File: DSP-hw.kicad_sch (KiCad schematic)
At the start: 0 parts

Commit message: Iniziata un po la schematica
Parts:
- added C1, C12, C14, C16, C18, C21, C3, C6, C9: 100n, Capacitor_SMD:C_0603_1608Metric, symbol Device:C
- added C10, C13, C15, C17, C2, C4, C5, C8: 10u, Capacitor_SMD:C_0603_1608Metric, symbol Device:C
- added C11, C7: 1u, Capacitor_SMD:C_0603_1608Metric, symbol Device:C
- added C19, C20: 47u, Capacitor_SMD:C_0603_1608Metric, symbol Device:C
- added C22, C23: 22p, Capacitor_SMD:C_0603_1608Metric, symbol Device:C
- added Q1: BC327, Package_TO_SOT_THT:TO-92_Inline, symbol Transistor_BJT:BC327
- added R1: 1k, Resistor_SMD:R_0603_1608Metric, symbol Device:R
- added R2, R3, R7: 33, Resistor_SMD:R_0603_1608Metric, symbol Device:R
- added R4: 2k2, Resistor_SMD:R_0603_1608Metric, symbol Device:R
- added R5: 18k, Resistor_SMD:R_0603_1608Metric, symbol Device:R
- added R6: 100, Resistor_SMD:R_0603_1608Metric, symbol Device:R
- added R8: 10k, Resistor_SMD:R_0603_1608Metric, symbol Device:R
- added SW1: SW_Push, Button_Switch_SMD:SW_SPST_PTS645Sx43SMTR92, symbol Switch:SW_Push
- added U1: ADAU1701, Package_QFP:LQFP-48_7x7mm_P0.5mm, symbol DSP_AnalogDevices:ADAU1701
- added U2: CAT24C256, Package_SO:SOIC-8_3.9x4.9mm_P1.27mm, symbol Memory_EEPROM:CAT24C256
- added U3: AMS1117-3.3, Package_TO_SOT_SMD:SOT-223-3_TabPin2, symbol Regulator_Linear:AMS1117-3.3
- added Y1: 12.228M, Crystal:Crystal_SMD_HC49-SD, symbol Device:Crystal
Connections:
- new net: R2.1, U2.5 (SDA)
- new net: R3.1, U2.6 (SCL)
- new net: C16.1, C17.1, U1.40 (CM)
- new net: C23.2, R6.1, Y1.2
- new net: R6.2, U1.31 (OSCO)
- new net: C5.2, C6.2, C7.2, C8.2, U1.34 (PVDD), U1.36 (AVDD), U1.48 (AVDD)
- new net: R5.2, U1.3 (ADC_RES)
- new net: R7.1, R8.1, SW1.2
- new net: R7.2, U1.5 (~{RESET})
- new net: C1.1, C2.1, C3.1, C4.1, Q1.1 (C), U1.13 (DVDD), U1.24 (DVDD)
- new net: C22.2, U1.32 (MCLKI), Y1.1
- new net: C14.1, C15.1, U1.47 (FILTA)
- new net: C12.1, C13.1, U1.41 (FILTD)
- new net +3V3: C10.2, C11.2, C18.1, C19.1, C9.2, Q1.2 (B), Q1.3 (E), R1.1, R1.2, R4.1, R8.2, U1.17 (VDRIVE), U1.18 (IOVDD), U1.39 (PLL_MODE1), U1.6 (SELFBOOT), U2.8 (VCC), U3.2 (VO)
- new net +5V: C20.1, C21.1, U3.3 (VI)
- new net ADC0: U1.2 (ADC0)
- new net ADC1: U1.4 (ADC1)
- new net BCLK: U1.9 (MP5)
- new net DAC0: U1.46 (VOUT0)
- new net DAC1: U1.45 (VOUT1)
- new net DAC2: U1.44 (VOUT2)
- new net DAC3: U1.43 (VOUT3)
- new net DIN: U1.15 (MP6)
- new net DOUT: U1.11 (MP0)
- new net GND: C1.2, C10.1, C11.1, C12.2, C13.2, C14.2, C15.2, C16.2, C17.2, C18.2, C19.2, C2.2, C20.2, C21.2, C22.1, C23.1, C3.2, C4.2, C5.1, C6.1, C7.1, C8.1, C9.1, R5.1, SW1.1, U1.1 (AGND), U1.12 (DGND), U1.25 (DGND), U1.30 (RSVD), U1.33 (PGND), U1.37 (AGND), U1.38 (PLL_MODE0), U1.42 (AGND), U1.7 (ADDR0), U2.1 (A0), U2.2 (A1), U2.3 (A2), U2.4 (GND), U3.1 (GND)
- new net LRCLK: U1.8 (MP4)
- new net SCL: R3.2, U1.23 (SCL/CCLK)
- new net SDA: R2.2, U1.22 (SDA/COUT)
- new net WP: R4.2, U1.21 (CLATCH/WP), U2.7 (WP)

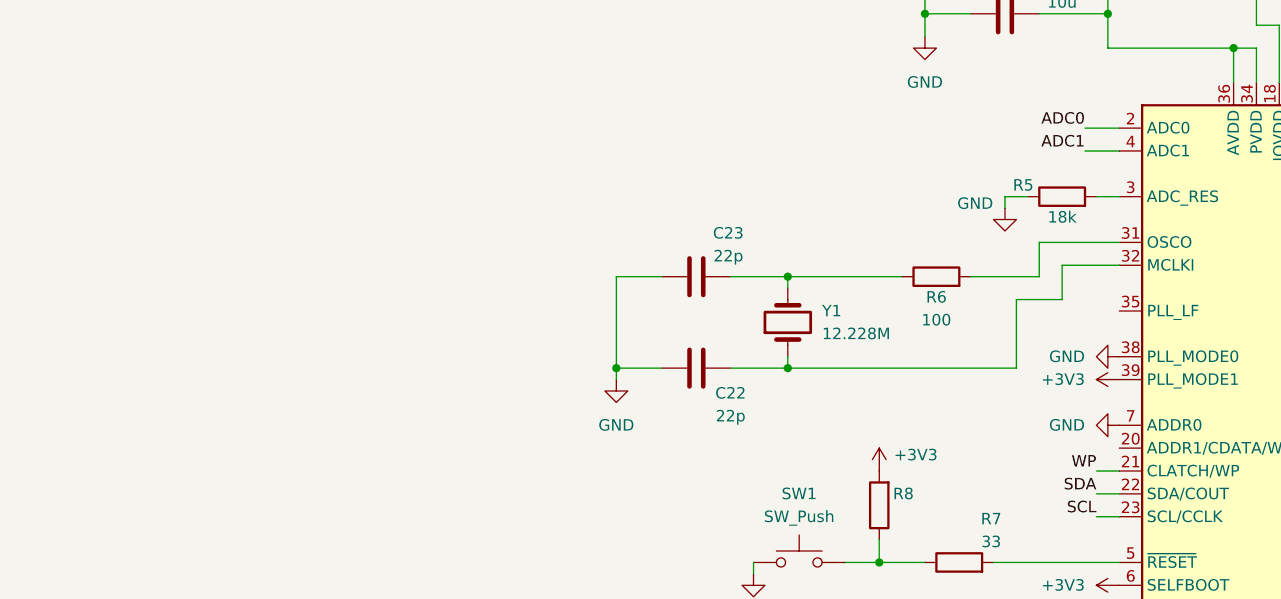
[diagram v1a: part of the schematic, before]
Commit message: aggiunto filtro PLL_LF Adau
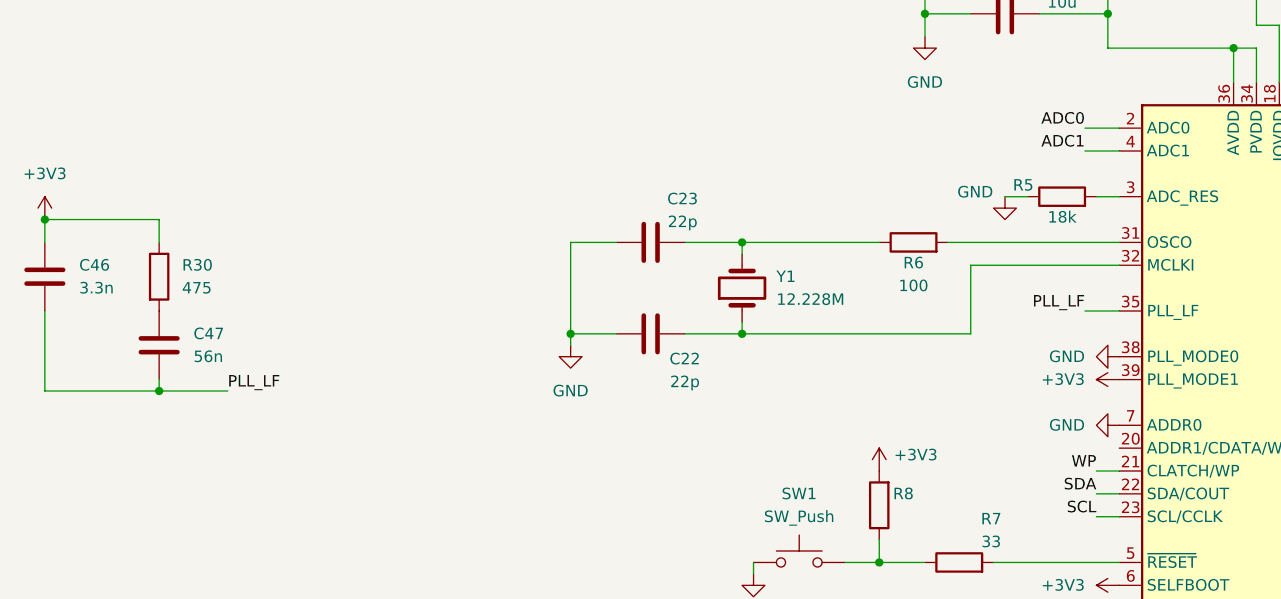
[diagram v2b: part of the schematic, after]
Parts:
- added C46: 3.3n, Capacitor_SMD:C_0603_1608Metric, symbol Device:C
- added C47: 56n, Capacitor_SMD:C_0603_1608Metric, symbol Device:C
- added R30: 475, Resistor_SMD:R_0603_1608Metric, symbol Device:R
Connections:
- net +3V3: now also C46.1, R30.1
- net PLL_LF: now reaches U1.35 (PLL_LF)
- net PLL_LF: now also C46.2, C47.2
- new net: C47.1, R30.2
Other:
- moved on the sheet: C22, C23, R6, Y1

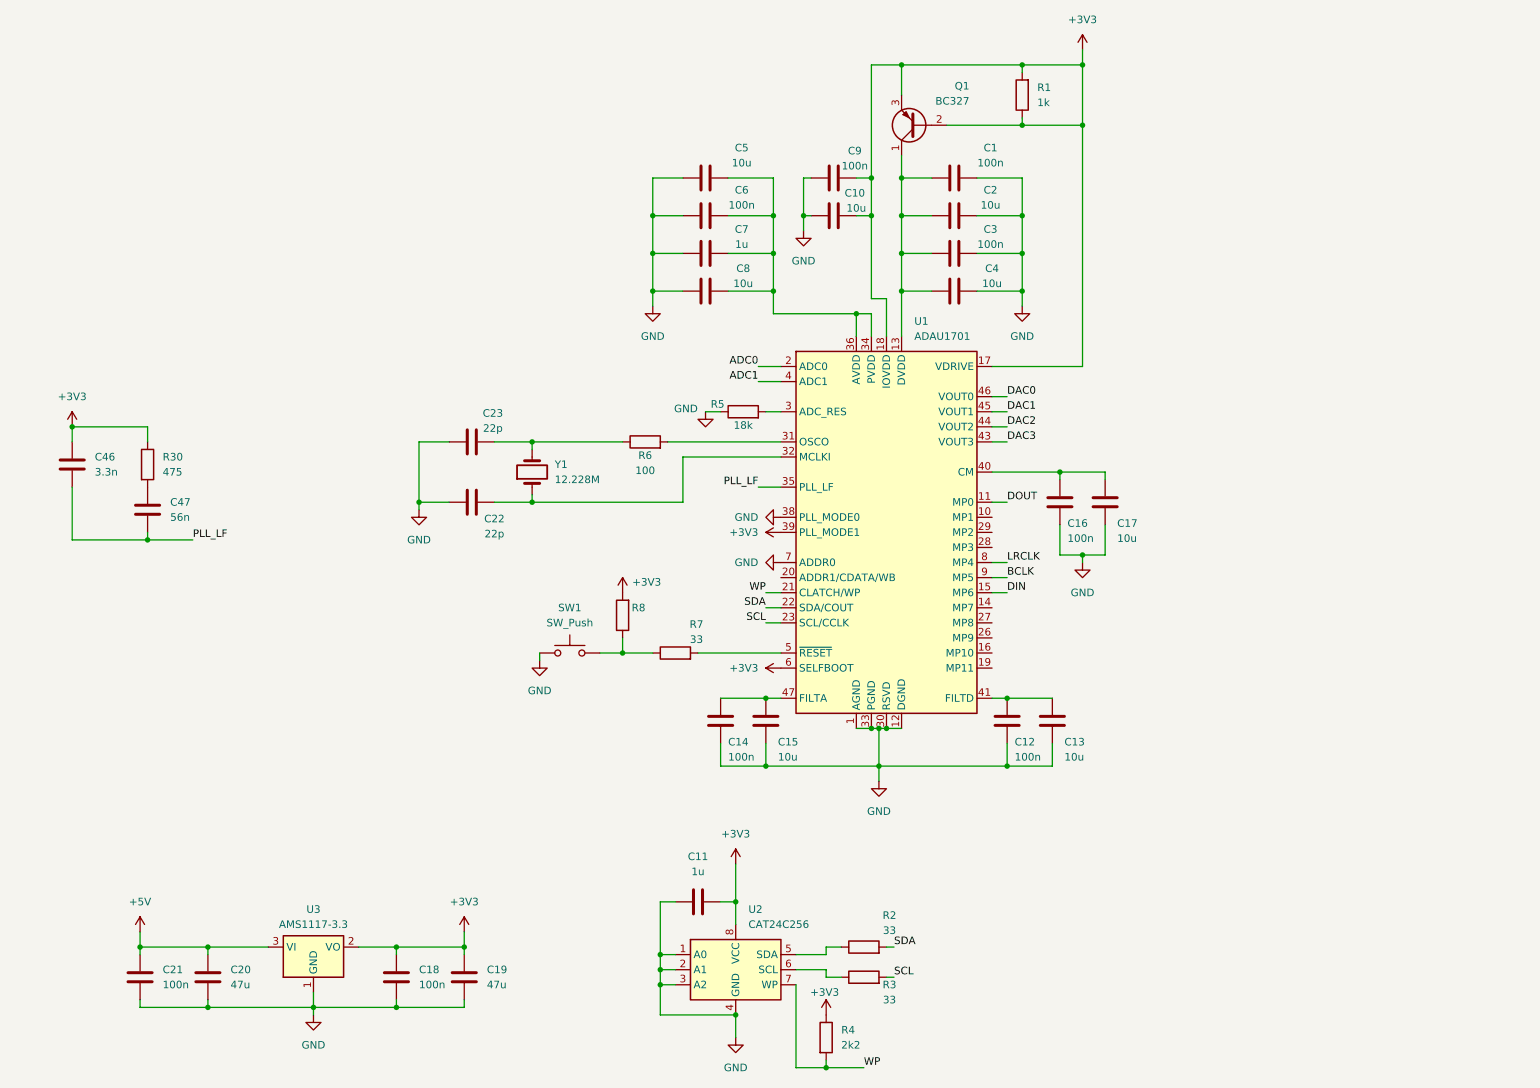
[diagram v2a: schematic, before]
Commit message: sostituito micro esp32 a stm32
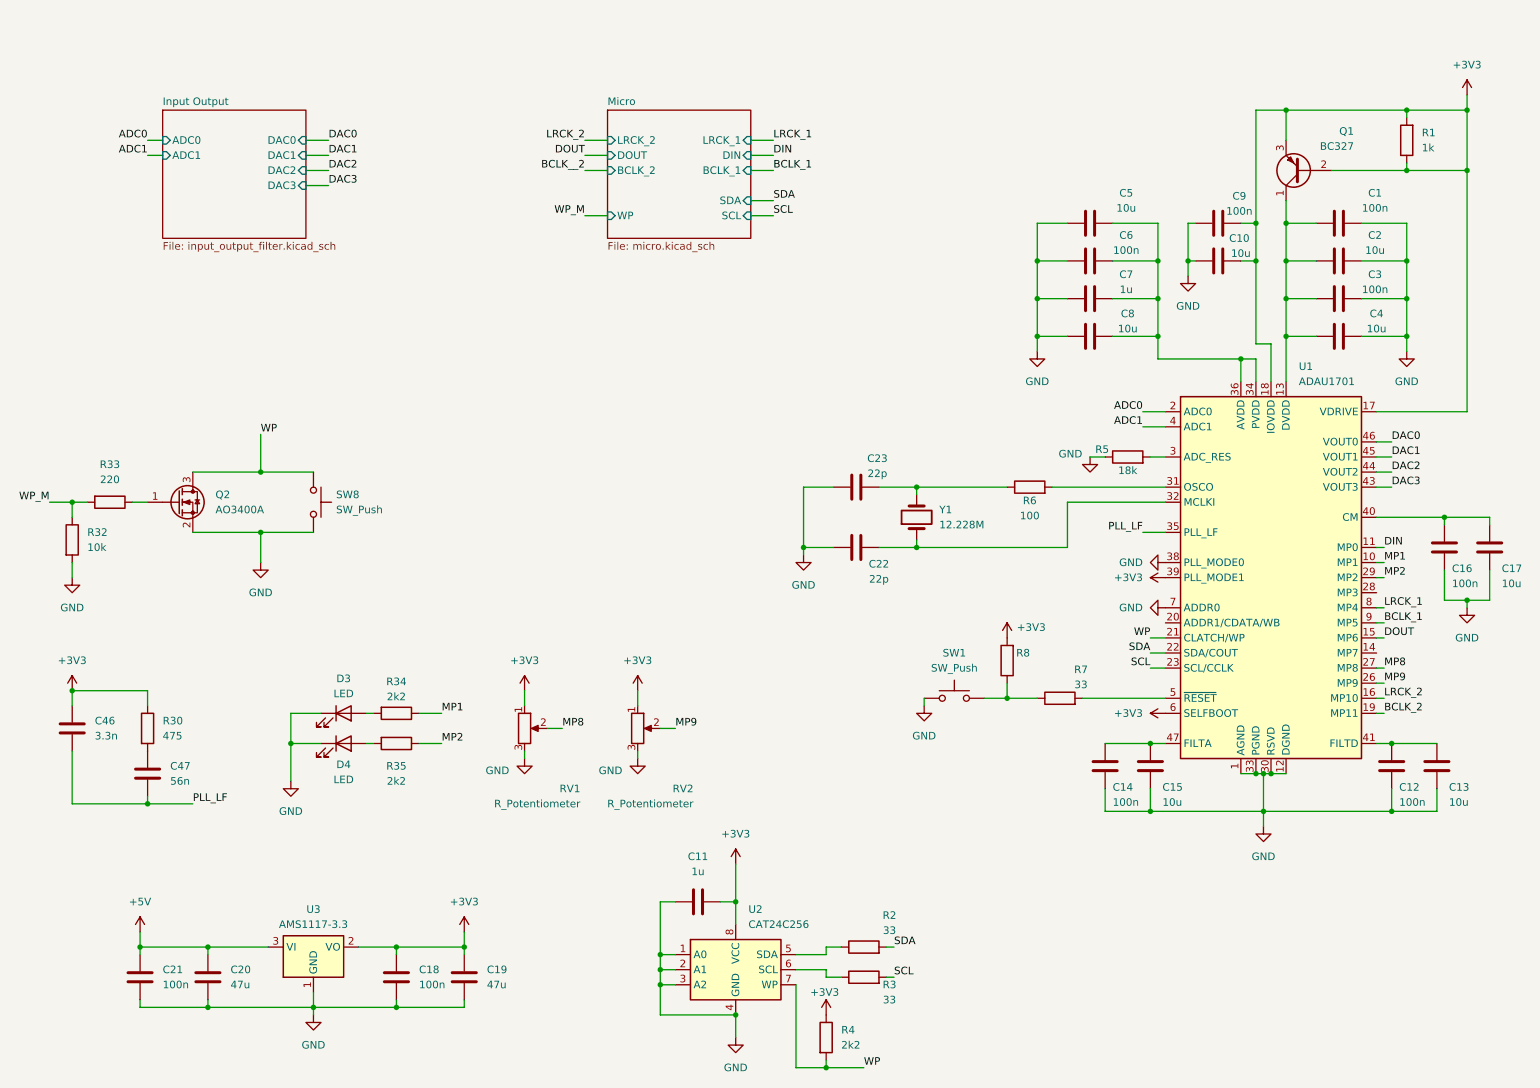
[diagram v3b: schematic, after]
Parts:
- added D3, D4: LED, LED_SMD:LED_1210_3225Metric, symbol Device:LED
- added Q2: AO3400A, Package_TO_SOT_SMD:SOT-23, symbol Transistor_FET:AO3400A
- added R32: 10k, Resistor_SMD:R_0603_1608Metric, symbol Device:R
- added R33: 220, Resistor_SMD:R_0603_1608Metric, symbol Device:R
- added R34, R35: 2k2, Resistor_SMD:R_0603_1608Metric, symbol Device:R
- added RV1, RV2: R_Potentiometer, Potentiometer_THT:Potentiometer_Alps_RK097_Single_Horizontal, symbol Device:R_Potentiometer
- added SW8: SW_Push, Button_Switch_SMD:SW_SPST_PTS645Sx43SMTR92, symbol Switch:SW_Push
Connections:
- net +3V3: now also RV1.1, RV2.1
- net DIN: now also U1.11 (MP0); no longer U1.15 (MP6)
- net DOUT: now also U1.15 (MP6); no longer U1.11 (MP0)
- net GND: now also D3.1 (K), D4.1 (K), Q2.2 (S), R32.2, RV1.3, RV2.3, SW8.2
- net WP: now also Q2.3 (D), SW8.1
- net MP1: now reaches U1.10 (MP1)
- net MP1: now also R34.1
- net LRCK_2: now reaches U1.16 (MP10)
- net BCLK_2: now reaches U1.19 (MP11)
- net MP9: now reaches U1.26 (MP9)
- net MP9: now also RV2.2
- net MP8: now reaches U1.27 (MP8)
- net MP8: now also RV1.2
- net MP2: now reaches U1.29 (MP2)
- net MP2: now also R35.1
- net BCLK renamed BCLK_1
- net LRCLK renamed LRCK_1
- new net: Q2.1 (G), R33.1
- new net: D3.2 (A), R34.2
- new net: D4.2 (A), R35.2
- new net WP_M: R32.1, R33.2
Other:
- added sheet Input Output (input_output_filter.kicad_sch)
- added sheet Micro (micro.kicad_sch)
- moved on the sheet: C1, C10, C12, C13, C14, C15, C16, C17, C2, C22, C23, C3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
